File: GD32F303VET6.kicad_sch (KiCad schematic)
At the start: 39 parts, among them SW1 SKRPACE010, U26 ESP32-C3-WROOM-02U-N4, U27 ESP32-C3-WROOM-02U-N4, U7 GD32F303VET6, U8 GD25Q16ESIGR, Y1 TAXM8M4RDBCCT2T, Y2 XKXGI-SUA-32.768K

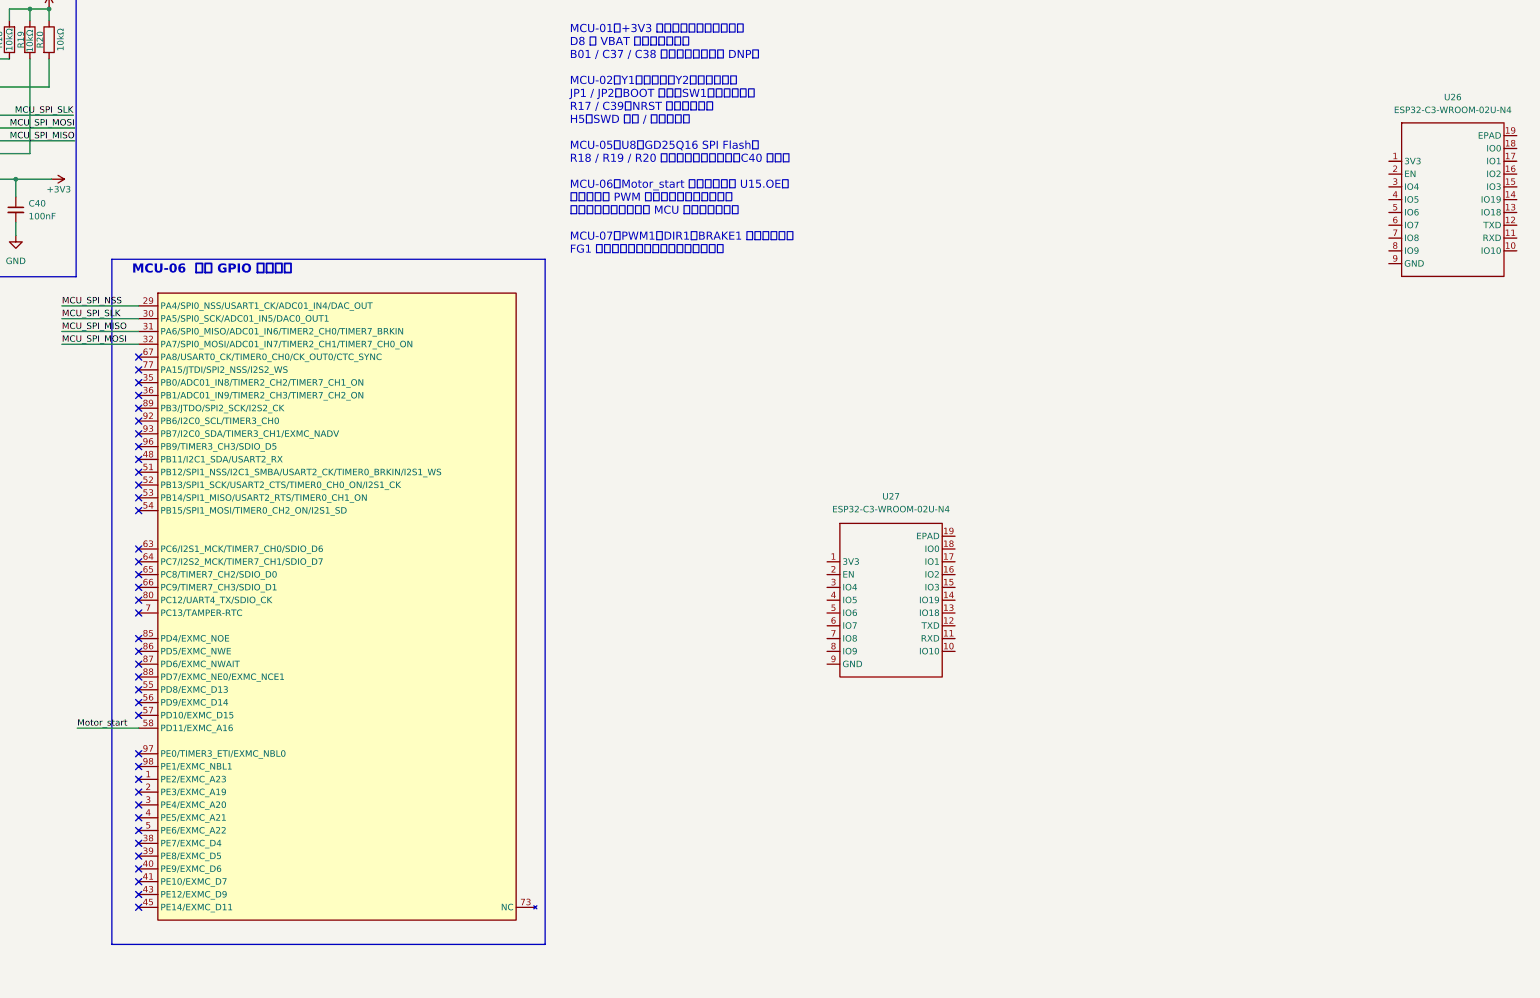
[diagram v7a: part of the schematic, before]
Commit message: V2.0: add minimal ESP32-C3 Wi-Fi OTA hardware and save current PCB layout
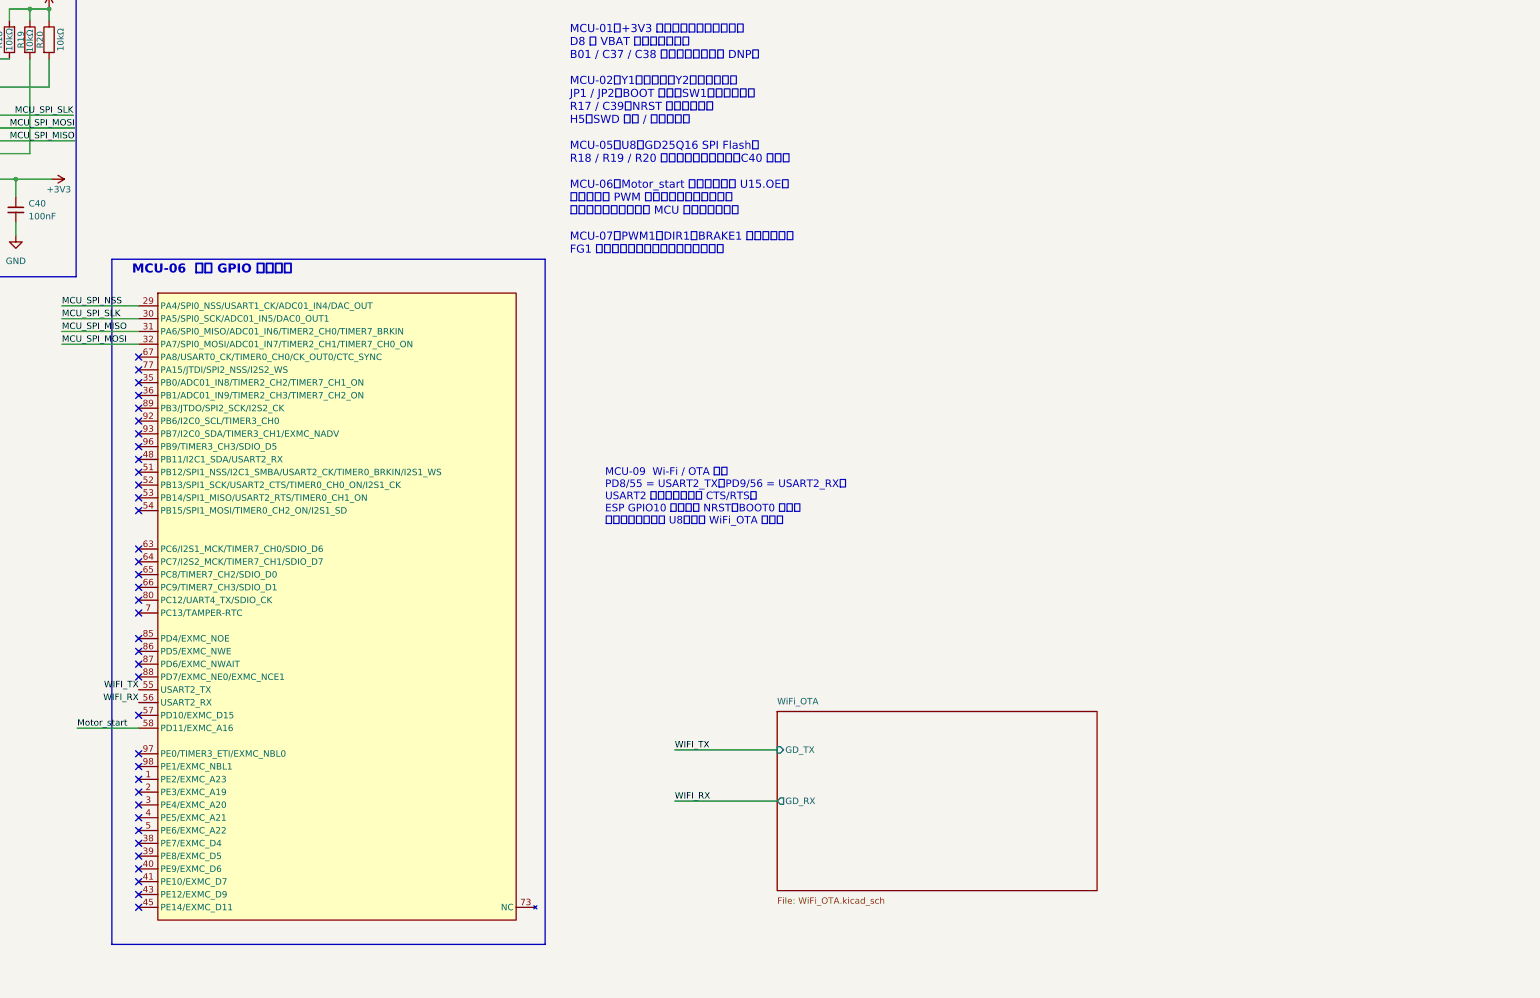
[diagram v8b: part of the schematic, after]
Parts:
- removed U26, U27: ESP32-C3-WROOM-02U-N4, kicad_api_lib:ESP32-C3-WROOM-02U-N4, symbol ESP32-C3-WROOM-02U-N4:ESP32-C3-WROOM-02U-N4
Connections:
- net WIFI_TX: now reaches U7.55 (PD8/EXMC_D13)
- net WIFI_RX: now reaches U7.56 (PD9/EXMC_D14)
- no-connect marks 41 -> 39
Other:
- added sheet WiFi_OTA (WiFi_OTA.kicad_sch)
- note added: "MCU-09 Wi-Fi / OTA 接口 PD8/55 = USART2_TX；PD9/56 = USART2_RX。 USART2 全重映射；关闭 CTS/RTS。 ESP GPIO10 开漏控制 NRST；BOOT0 不变。 升级缓存使用现有 U8，详见 WiFi_OTA 子页。"
